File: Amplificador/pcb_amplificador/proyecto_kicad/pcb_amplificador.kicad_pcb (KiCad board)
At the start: 2 copper layers, 149.9 x 88.9 mm, 139 parts, among them CON1 SJ-3523-SMT-TR, J1 Screw_Terminal_01x02, J2 Screw_Terminal_01x02, J3 Screw_Terminal_01x02, J4 Screw_Terminal_01x02, J5 Conn_01x03_Male, J6 Screw_Terminal_01x02, J7 Screw_Terminal_01x02, K1 FINDER-40.11-2016, M1 FDS9934C, M2 FDS9934C, Q1 BC860, Q10 BD139, Q11 BD140, Q12 BD139, Q13 2SA1943-O_Q_, Q14 2SC5200-O_Q, Q15 2SA1943-O_Q_, Q16 2SC5200-O_Q, Q17 2SAR514P5, Q18 BC860, Q19 BC860, Q2 BC860, Q20 2SAR514P5, Q21 2SCR514P5, Q22 2SCR514P5, Q23 2SCR514P5, Q24 2SAR514P5, Q25 2SCR514P5, Q26 BC817, Q27 BC817, Q28 BC807, Q29 BS170, Q3 BC850, Q4 BC850, Q5 BC860, Q6 BC860, Q7 BC850, Q8 2SCR514P5, Q9 2SCR514P5

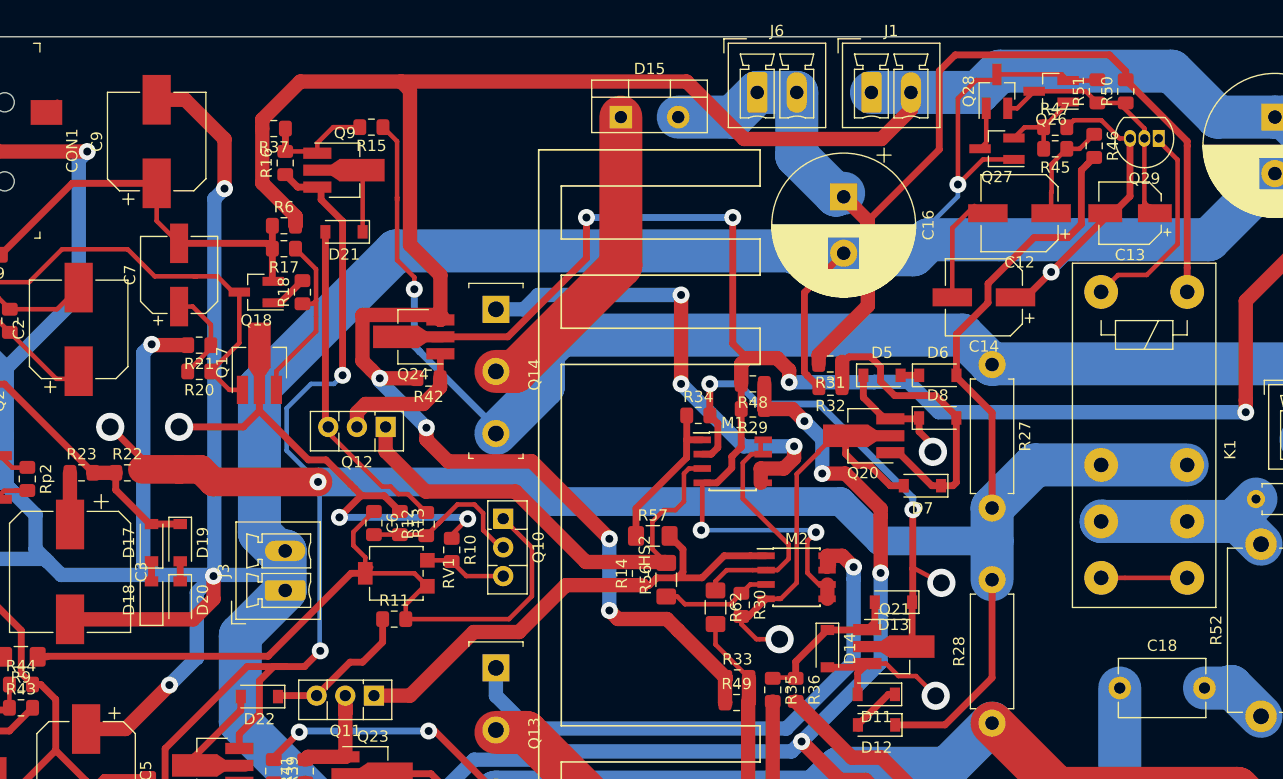
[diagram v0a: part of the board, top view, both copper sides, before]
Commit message: Agregado de datos extra de los componentes en el esquemático del amplificador y cambios menores
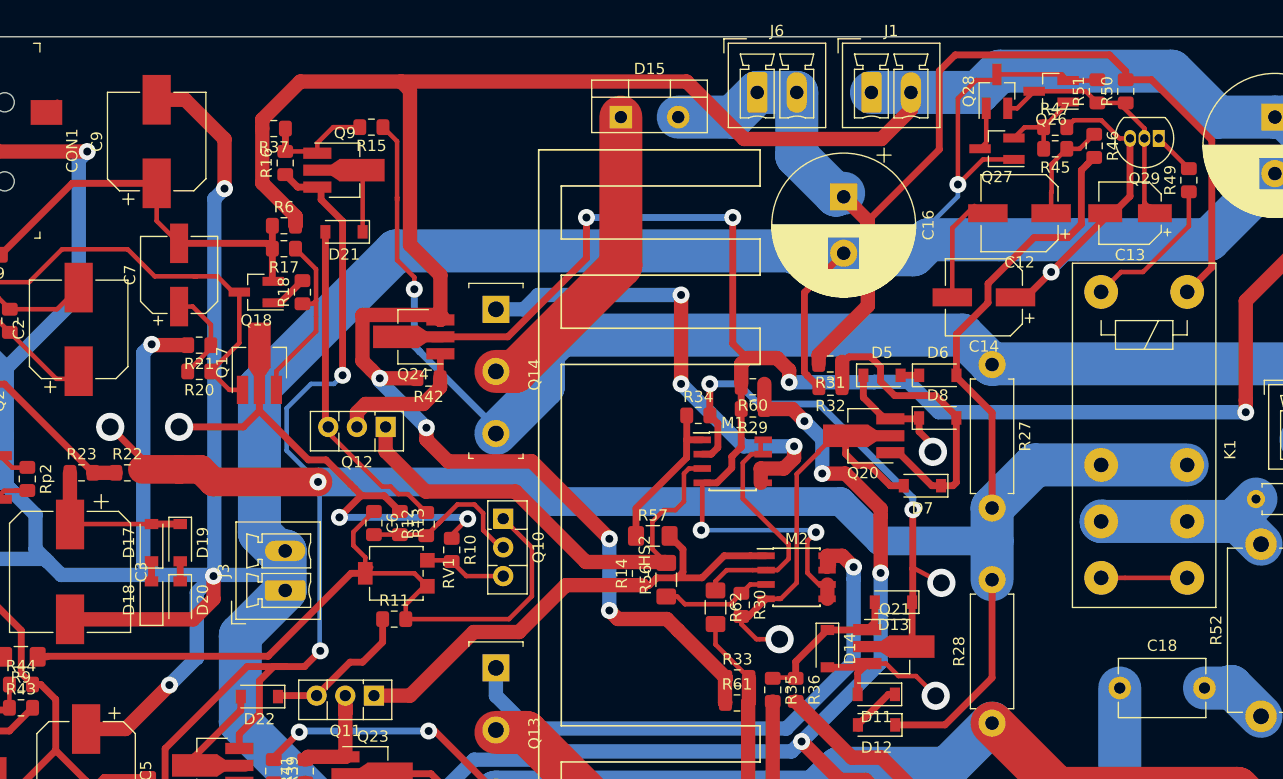
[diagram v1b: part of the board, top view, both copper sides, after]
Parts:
- removed R48: 10k, Resistor_SMD:R_0805_2012Metric_Pad1.15x1.40mm_HandSolder
- added R60: 10k, Resistor_SMD:R_0805_2012Metric_Pad1.15x1.40mm_HandSolder, F.Cu at (113.5, 83.1)
- added R61: 10k, Resistor_SMD:R_0805_2012Metric_Pad1.15x1.40mm_HandSolder, F.Cu at (112.1, 111.1)
- C6: value 33n -> 39n
- R10: value 2k -> 2.2k
- R13: value 16 -> 22
- R32, R36: value 3k -> 2.7k
- R49: value 10k -> 12k
- moved R49 61.2 mm to (152.1, 64.8), turned to 90 degrees
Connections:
- D17 pad 2: Net-(D17-Pad2) -> Net-(C3-Pad1)
- D19 pad 1: Net-(D17-Pad2) -> Net-(C3-Pad1)
- J4 pad 2: Net-(J4-Pad2) -> Net-(J4-Pad1)
- Q2 pad 1: Net-(D17-Pad2) -> Net-(Q2-Pad1)
- Q29 pad 1: Net-(K1-PadA2) -> Net-(Q29-Pad1)
- R22 pad 1: Net-(D17-Pad2) -> Net-(Q2-Pad1)
- R23 pad 2: Net-(D17-Pad2) -> Net-(Q2-Pad1)
- R24 pad 1: Net-(D17-Pad2) -> Net-(Q2-Pad1)
- R49 pad 1: /Vmax -> Net-(K1-PadA2)
- R49 pad 2: Net-(D9-Pad2) -> Net-(Q29-Pad1)
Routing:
- net Net-(D17-Pad2): track 28.8 -> 0.00 mm
- net Net-(Q2-Pad1): track 0.00 -> 19.9 mm
- net Net-(C3-Pad1): track 5.71 -> 16.0 mm
- net Net-(K1-PadA2): track 18.6 -> 13.2 mm
- net Net-(Q29-Pad1): track 0.00 -> 4.01 mm
- net /Vmin: track 95.6 -> 98.7 mm

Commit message: Agregado de los resultados de la medicion de la proteccion de DC
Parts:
- removed R49: 12k, Resistor_SMD:R_0805_2012Metric_Pad1.15x1.40mm_HandSolder
- added D1: 1N4148W, Diode_SMD:D_SOD-123, F.Cu at (154.2, 70.1)
- moved Q4 0.27 mm to (45.2, 93.0)
- moved Q6 0.27 mm to (45.2, 89.2)
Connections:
- K1 pad 12: /VOUT -> Net-(K1-Pad12)
- K1 pad 14: Net-(K1-Pad14) -> /VOUT
- K1 pad A2: Net-(K1-PadA2) -> Net-(D1-Pad2)
- Q29 pad 1: Net-(Q29-Pad1) -> Net-(D1-Pad2)
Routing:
- net Net-(D1-Pad2): track 0.00 -> 21.2 mm
- net Net-(K1-PadA2): track 13.2 -> 0.00 mm
- net Net-(K1-Pad14): track 7.62 -> 0.00 mm
- net Net-(K1-Pad12): track 0.00 -> 7.62 mm
- net Net-(Q29-Pad1): track 4.01 -> 0.00 mm
- net /VOUT: track 251.3 -> 249.7 mm
- net /Vmin: track 98.7 -> 99.5 mm

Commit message: Agregado de los resultados de las mediciones de THD con las protecciones y desarrollo de la explicación del comportamiento de los limitadores de corriente en el semicilo negativo
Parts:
- R37, R40: value 15k -> 11k
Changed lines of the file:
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@@
-(kicad_pcb (version 20171130) (host pcbnew 5.1.2-f72e74a~84~ubuntu18.04.1)
+(kicad_pcb (version 20171130) (host pcbnew "(5.0.1)-4")
   (general
     (thickness 1.6)
@@
     (zone_45_only no)
     (trace_min 0.3048)
+    (segment_width 0.2)
+    (edge_width 0.05)
     (via_size 1.5)
     (via_drill 0.7)
@@
     (uvia_min_size 0.2)
     (uvia_min_drill 0.1)
-    (edge_width 0.05)
-    (segment_width 0.2)
     (pcb_text_width 0.3)
     (pcb_text_size 1.5 1.5)
@@
     (uvia_dia 0.3)
     (uvia_drill 0.1)
+    (diff_pair_gap 0.25)
     (diff_pair_width 0.4064)
-    (diff_pair_gap 0.25)
     (add_net /-Vmax)
     (add_net /-Vmin)
@@
       (effects (font (size 1 1) (thickness 0.15)))
     )
-    (fp_text value 15k (at 0 1.65 180) (layer F.Fab)
+    (fp_text value 11k (at 0 1.65 180) (layer F.Fab)
       (effects (font (size 1 1) (thickness 0.15)))
     )
@@
       (effects (font (size 1 1) (thickness 0.15)))
     )
-    (fp_text value 15k (at 0 1.65 180) (layer F.Fab)
-      (effects (font (size 1 1) (thickness 0.15)))
-    )
+    (fp_text value 11k (at 0 1.65 180) (layer F.Fab)
+      (effects (font (size 1 1) (thickness 0.15)))
+    )

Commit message: Agregado de las mediciones finales y algunos cambios menores
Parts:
- Q13, Q14, Q15, Q16: footprint digikey-footprints:TO-3P-5 -> Package_TO_SOT_THT:TO-264-3_Vertical
